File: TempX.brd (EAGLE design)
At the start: 30.5 x 7.6 mm, 6 parts, among them U1 TMP36

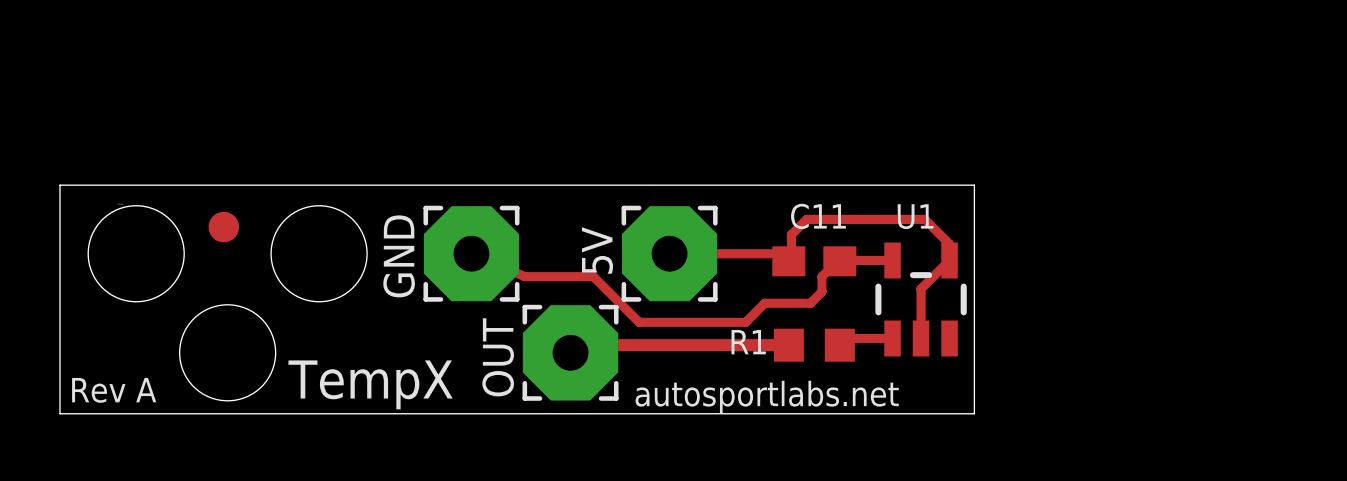
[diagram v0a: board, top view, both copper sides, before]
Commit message: made board slimmer
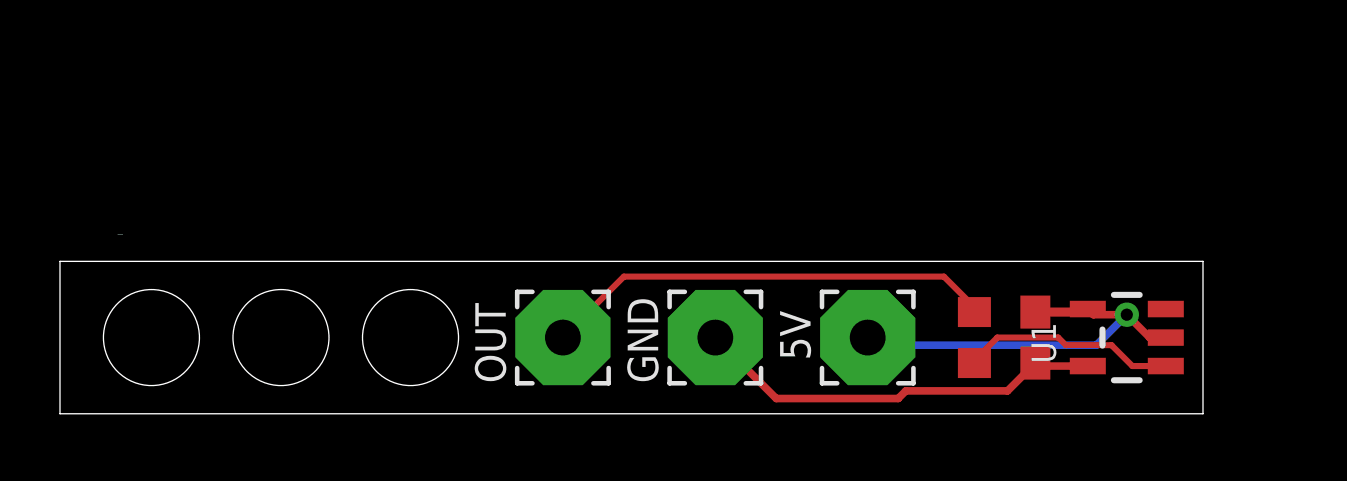
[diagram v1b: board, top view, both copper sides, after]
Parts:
- moved GND 8.59 mm to (21.8, 2.54)
- moved C11 7.79 mm to (32.5, 2.54), turned to 270 degrees
- moved 5V 7.17 mm to (26.9, 2.54)
- moved U1 6.97 mm to (35.6, 2.54), turned to 90 degrees
- moved R1 5.34 mm to (30.5, 2.54), turned to 270 degrees
- moved OUT 0.57 mm to (16.8, 2.54)
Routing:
- net N$1: track 7.31 -> 15.1 mm
- net N$2: track 1.85 -> 7.18 mm
- net C1: track 16.0 -> 13.8 mm
- net 5V: track 14.4 -> 14.0 mm, vias 0 -> 1
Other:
- board size 30.5 x 7.6 mm -> 38.1 x 5.1 mm
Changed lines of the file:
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@@
 <board>
 <plain>
-<wire x1="0" y1="0" x2="30.48" y2="0" width="0" layer="20"/>
-<wire x1="30.48" y1="0" x2="30.48" y2="7.62" width="0" layer="20"/>
-<wire x1="30.48" y1="7.62" x2="0" y2="7.62" width="0" layer="20"/>
-<wire x1="0" y1="7.62" x2="0" y2="0" width="0" layer="20"/>
-<text x="19.1262" y="0.254" size="0.8128" layer="21" font="vector">autosportlabs.net</text>
-<text x="0.3048" y="0.381" size="0.8128" layer="21" font="vector">Rev A</text>
-<text x="7.62" y="0.508" size="1.27" layer="21">TempX</text>
-<rectangle x1="1.9215" y1="6.9838" x2="2.0993" y2="6.9964" layer="21"/>
-<hole x="5.588" y="2.032" drill="3.2"/>
-<hole x="8.636" y="5.334" drill="3.2"/>
-<hole x="2.54" y="5.334" drill="3.2"/>
-<circle x="5.461" y="6.223" radius="0.508" width="0" layer="1"/>
-<circle x="5.461" y="6.223" radius="1.016" width="0" layer="29"/>
+<wire x1="0" y1="0" x2="38.1" y2="0" width="0" layer="20"/>
+<wire x1="38.1" y1="0" x2="38.1" y2="5.08" width="0" layer="20"/>
+<wire x1="38.1" y1="5.08" x2="0" y2="5.08" width="0" layer="20"/>
+<wire x1="0" y1="5.08" x2="0" y2="0" width="0" layer="20"/>
+<text x="37.9222" y="0.254" size="0.762" layer="22" font="vector" rot="MR0">autosportlabs.net</text>
+<text x="1.143" y="4.3688" size="0.8128" layer="22" font="vector" rot="MR270">Rev A</text>
+<text x="37.846" y="3.556" size="1.27" layer="22" rot="MR0">TempX</text>
+<rectangle x1="1.9215" y1="5.9678" x2="2.0993" y2="5.9804" layer="21"/>
+<hole x="7.366" y="2.54" drill="3.2"/>
+<hole x="11.684" y="2.54" drill="3.2"/>
+<hole x="3.048" y="2.54" drill="3.2"/>
 </plain>
 <attributes>
@@
 </class>
 </classes>
-<designrules name="default">
+<designrules name="default *">
 <description language="de">&lt;b&gt;EAGLE Design Rules&lt;/b&gt;
 &lt;p&gt;
@@
 <param name="mlMinCreamFrame" value="0mil"/>
 <param name="mlMaxCreamFrame" value="0mil"/>
-<param name="mlViaStopLimit" value="0mil"/>
+<param name="mlViaStopLimit" value="16mil"/>
 <param name="srRoundness" value="0"/>
 <param name="srMinRoundness" value="0mil"/>
@@
 </autorouter>
 <elements>
-<element name="GND" library="wirepad" package="3,17/1,2" value="WIREPAD3,17/1,2" x="13.716" y="5.334" smashed="yes">
-<attribute name="NAME" x="11.811" y="3.81" size="1.016" layer="25" ratio="10" rot="R90"/>
-<attribute name="VALUE" x="13.716" y="6.534" size="0.0254" layer="27"/>
-</element>
-<element name="5V" library="wirepad" package="3,17/1,2" value="WIREPAD3,17/1,2" x="20.32" y="5.334" smashed="yes">
-<attribute name="NAME" x="18.415" y="4.572" size="1.016" layer="25" ratio="10" rot="R90"/>
-<attribute name="VALUE" x="20.32" y="6.534" size="0.0254" layer="27"/>
-</element>
-<element name="OUT" library="wirepad" package="3,17/1,2" value="WIREPAD3,17/1,2" x="17.018" y="2.032" smashed="yes">
-<attribute name="NAME" x="15.113" y="0.508" size="1.016" layer="25" ratio="10" rot="R90"/>
-<attribute name="VALUE" x="17.018" y="3.232" size="0.0254" layer="27"/>
-</element>
-<element name="U1" library="TMP36" package="SOT-23" value="TMP36" x="28.702" y="3.81" smashed="yes">
-<attribute name="NAME" x="29.21" y="6.985" size="0.8128" layer="25" rot="R180"/>
-</element>
-<element name="R1" library="rcl" package="R0603" value="1K" x="25.146" y="2.286" smashed="yes">
-<attribute name="NAME" x="23.622" y="2.794" size="0.8128" layer="25" rot="R180"/>
-</element>
-<element name="C11" library="rcl" package="C0603" value="0.1uF" x="25.146" y="5.08" smashed="yes">
-<attribute name="NAME" x="26.289" y="6.985" size="0.8128" layer="25" rot="R180"/>
-</element>
+<element name="GND" library="wirepad" package="3,17/1,2" value="WIREPAD3,17/1,2" x="21.844" y="2.54" smashed="yes">
+<attribute name="NAME" x="19.939" y="1.016" size="1.016" layer="25" ratio="10" rot="R90"/>
+<attribute name="VALUE" x="21.844" y="3.74" size="0.0254" layer="27"/>
+</element>
+<element name="5V" library="wirepad" package="3,17/1,2" value="WIREPAD3,17/1,2" x="26.924" y="2.54" smashed="yes">
+<attribute name="NAME" x="25.019" y="1.778" size="1.016" layer="25" ratio="10" rot="R90"/>
+<attribute name="VALUE" x="26.924" y="3.74" size="0.0254" layer="27"/>
+</element>
+<element name="OUT" library="wirepad" package="3,17/1,2" value="WIREPAD3,17/1,2" x="16.764" y="2.54" smashed="yes">
+<attribute name="NAME" x="14.859" y="1.016" size="1.016" layer="25" ratio="10" rot="R90"/>
+<attribute name="VALUE" x="16.764" y="3.74" size="0.0254" layer="27"/>
+</element>
+<element name="U1" library="TMP36" package="SOT-23" value="TMP36" x="35.56" y="2.54" smashed="yes" rot="R90">
+<attribute name="NAME" x="32.385" y="3.048" size="0.8128" layer="25" rot="R270"/>
+</element>
+<element name="R1" library="rcl" package="R0603" value="1K" x="30.48" y="2.54" smashed="yes" rot="R270"/>
+<element name="C11" library="rcl" package="C0603" value="0.1uF" x="32.512" y="2.54" smashed="yes" rot="R270"/>
 </elements>
 <signals>
@@
 <contactref element="R1" pad="1"/>
 <contactref element="OUT" pad="1"/>
-<wire x1="24.296" y1="2.286" x2="18.034" y2="2.286" width="0.4064" layer="1"/>
-<wire x1="18.034" y1="2.286" x2="17.018" y2="2.032" width="0.4064" layer="1"/>
+<wire x1="30.48" y1="3.39" x2="30.392" y2="3.644" width="0.2032" layer="1"/>
+<wire x1="30.392" y1="3.644" x2="29.464" y2="4.572" width="0.2032" layer="1"/>
+<wire x1="29.464" y1="4.572" x2="18.796" y2="4.572" width="0.2032" layer="1"/>
+<wire x1="18.796" y1="4.572" x2="16.764" y2="2.54" width="0.2032" layer="1"/>
 </signal>
 <signal name="N$2">
 <contactref element="R1" pad="2"/>
 <contactref element="U1" pad="1"/>
-<wire x1="25.996" y1="2.286" x2="26.2199" y2="2.5099" width="0.3048" layer="1"/>
-<wire x1="26.2199" y1="2.5099" x2="27.752" y2="2.5099" width="0.3048" layer="1"/>
+<wire x1="31.242" y1="2.54" x2="30.48" y2="1.778" width="0.2032" layer="1"/>
+<wire x1="30.48" y1="1.778" x2="30.48" y2="1.69" width="0.254" layer="1"/>
+<wire x1="31.242" y1="2.54" x2="33.274" y2="2.54" width="0.2032" layer="1"/>
+<wire x1="33.274" y1="2.54" x2="33.528" y2="2.286" width="0.2032" layer="1"/>
+<wire x1="33.528" y1="2.286" x2="35.052" y2="2.286" width="0.2032" layer="1"/>
+<wire x1="35.052" y1="2.286" x2="35.748" y2="1.59" width="0.2032" layer="1"/>
+<wire x1="35.748" y1="1.59" x2="36.8601" y2="1.59" width="0.2032" layer="1"/>
 </signal>
 <signal name="5V">
@@
 <contactref element="U1" pad="4"/>
 <contactref element="U1" pad="2"/>
-<wire x1="29.652" y1="5.1101" x2="28.702" y2="4.1601" width="0.3048" layer="1"/>
-<wire x1="28.702" y1="4.1601" x2="28.702" y2="2.5099" width="0.3048" layer="1"/>
-<wire x1="24.296" y1="5.08" x2="24.384" y2="5.168" width="0.3048" layer="1"/>
-<wire x1="24.384" y1="5.168" x2="24.384" y2="5.969" width="0.3048" layer="1"/>
-<wire x1="24.384" y1="5.969" x2="24.892" y2="6.477" width="0.3048" layer="1"/>
-<wire x1="24.892" y1="6.477" x2="28.829" y2="6.477" width="0.3048" layer="1"/>
-<wire x1="28.829" y1="6.477" x2="29.652" y2="5.654" width="0.3048" layer="1"/>
-<wire x1="29.652" y1="5.654" x2="29.652" y2="5.1101" width="0.3048" layer="1"/>
-<wire x1="24.296" y1="5.08" x2="24.042" y2="5.334" width="0.3048" layer="1"/>
-<wire x1="24.042" y1="5.334" x2="20.32" y2="5.334" width="0.3048" layer="1"/>
+<wire x1="34.2599" y1="3.49" x2="34.1599" y2="3.39" width="0.3048" layer="1"/>
+<wire x1="34.1599" y1="3.39" x2="32.512" y2="3.39" width="0.3048" layer="1"/>
+<wire x1="34.1939" y1="3.556" x2="34.2599" y2="3.49" width="0.254" layer="1"/>
+<wire x1="34.544" y1="2.286" x2="35.56" y2="3.302" width="0.254" layer="16"/>
+<via x="35.56" y="3.302" extent="1-16" drill="0.4064"/>
+<wire x1="35.56" y1="3.302" x2="34.4479" y2="3.302" width="0.254" layer="1"/>
+<wire x1="34.4479" y1="3.302" x2="34.2599" y2="3.49" width="0.254" layer="1"/>
+<wire x1="36.8601" y1="2.54" x2="36.322" y2="2.54" width="0.254" layer="1"/>
+<wire x1="36.322" y1="2.54" x2="35.56" y2="3.302" width="0.254" layer="1"/>
+<wire x1="34.544" y1="2.286" x2="27.178" y2="2.286" width="0.254" layer="16"/>
+<wire x1="27.178" y1="2.286" x2="26.924" y2="2.54" width="0.254" layer="16"/>
 </signal>
 <signal name="C1">
@@
 <contactref element="C11" pad="2"/>
 <contactref element="U1" pad="5"/>
-<wire x1="13.716" y1="5.334" x2="15.494" y2="4.572" width="0.3048" layer="1"/>
-<wire x1="15.494" y1="4.572" x2="17.78" y2="4.572" width="0.3048" layer="1"/>
-<wire x1="17.78" y1="4.572" x2="19.304" y2="3.048" width="0.3048" layer="1"/>
-<wire x1="19.304" y1="3.048" x2="22.86" y2="3.048" width="0.3048" layer="1"/>
-<wire x1="22.86" y1="3.048" x2="23.495" y2="3.683" width="0.3048" layer="1"/>
-<wire x1="23.495" y1="3.683" x2="25.019" y2="3.683" width="0.3048" layer="1"/>
-<wire x1="25.019" y1="3.683" x2="25.4" y2="4.064" width="0.3048" layer="1"/>
-<wire x1="25.4" y1="4.064" x2="25.4" y2="4.572" width="0.3048" layer="1"/>
-<wire x1="25.4" y1="4.572" x2="25.908" y2="5.08" width="0.3048" layer="1"/>
-<wire x1="25.908" y1="5.08" x2="25.996" y2="5.08" width="0.3048" layer="1"/>
-<wire x1="25.996" y1="5.08" x2="26.0261" y2="5.1101" width="0.3048" layer="1"/>
-<wire x1="26.0261" y1="5.1101" x2="27.752" y2="5.1101" width="0.3048" layer="1"/>
+<wire x1="34.2599" y1="1.59" x2="32.612" y2="1.59" width="0.254" layer="1"/>
+<wire x1="32.612" y1="1.59" x2="32.512" y2="1.69" width="0.254" layer="1"/>
+<wire x1="27.94" y1="0.508" x2="28.194" y2="0.762" width="0.254" layer="1"/>
+<wire x1="28.194" y1="0.762" x2="31.584" y2="0.762" width="0.254" layer="1"/>
+<wire x1="31.584" y1="0.762" x2="32.512" y2="1.69" width="0.254" layer="1"/>
+<wire x1="27.94" y1="0.508" x2="23.876" y2="0.508" width="0.254" layer="1"/>
+<wire x1="23.876" y1="0.508" x2="21.844" y2="2.54" width="0.254" layer="1"/>
 </signal>
 </signals>

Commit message: changed design to circular
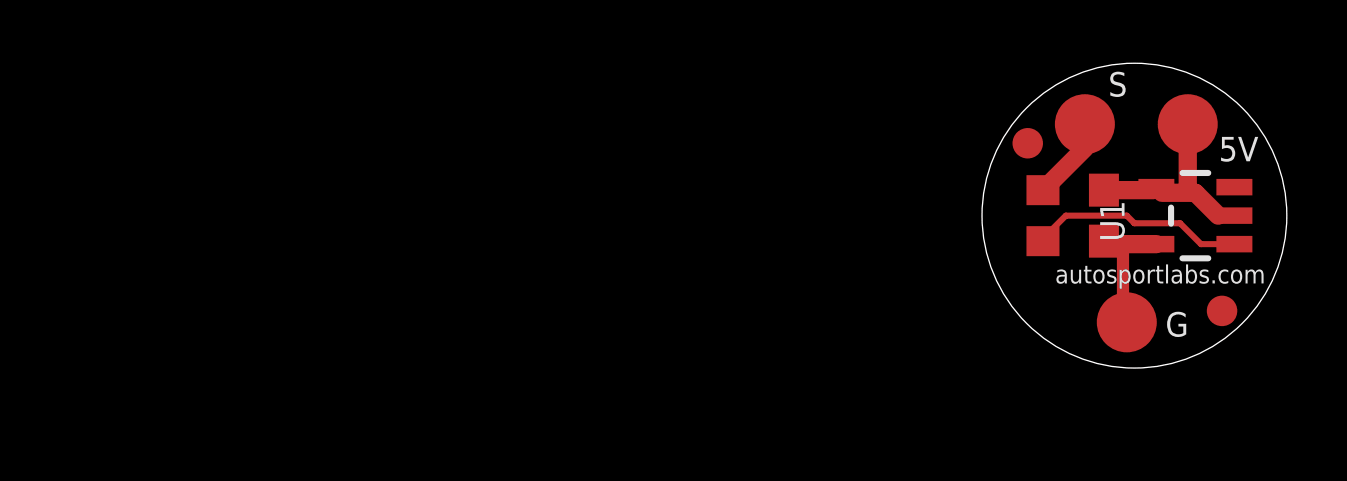
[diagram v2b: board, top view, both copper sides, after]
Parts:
- removed GND, OUT: WIREPAD3,17/1,2, wirepad:3,17/1,2
- added G, S: TPSQTP20R, testpad:TP20R
- 5V: value WIREPAD3,17/1,2 -> TPSQTP20R; device wirepad:3,17/1,2 -> testpad:TP20R
- moved 5V 12.8 mm to (37.6, 9.65)
- moved C11 4.66 mm to (34.8, 6.60)
- moved R1 4.66 mm to (32.8, 6.60)
- moved U1 4.66 mm to (37.8, 6.60)
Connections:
- net 5V: now also 5V.TP; no longer 5V.1
- net C1: now also G.TP; no longer GND.1
- net N$1: now also S.TP; no longer OUT.1
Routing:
- net N$1: track 15.1 -> 2.78 mm
- net C1: track 13.8 -> 4.41 mm
- net 5V: track 14.0 -> 7.27 mm, vias 1 -> 0
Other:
- board size 38.1 x 5.1 mm -> 10.2 x 10.2 mm
- board text added: "autosportlabs.com"
- board text removed: "autosportlabs.net"
